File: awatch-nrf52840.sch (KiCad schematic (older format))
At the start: 22 parts, among them U1 nRF52840, X1 ABM11W-32.0000MHZ-8-B1U-T3

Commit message: add sensors
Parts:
- added R?: n/c, symbol Device:R_Small_US
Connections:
- net +2V8: now also R?.1
- net SENS_IMU_INT: now reaches U1.R24 (P1.06)
- net SENS_IMU_INT: now also R?.2
- no-connect marks 19 -> 18
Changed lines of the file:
@@
 NoConn ~ 5150 5000
 NoConn ~ 5150 5200
-NoConn ~ 5150 5800
 NoConn ~ 5150 5900
 NoConn ~ 5150 6000
@@
 Wire Wire Line
 	5800 4950 5800 5000
+Text HLabel 6700 5800 2    50   Input ~ 0
+SENS_IMU_INT
+Wire Wire Line
+	5150 5800 6200 5800
+$Comp
+L Device:R_Small_US R?
+U 1 1 5C442EC0
+P 6200 5100
+F 0 "R?" H 6268 5146 50  0000 L CNN
+F 1 "n/c" H 6268 5055 50  0000 L CNN
+F 2 "" H 6200 5100 50  0001 C CNN
+F 3 "~" H 6200 5100 50  0001 C CNN
+	1    6200 5100
+	1    0    0    -1
+$EndComp
+$Comp
+L power:+2V8 #PWR?
+U 1 1 5C44AE8F
+P 6200 4950
+F 0 "#PWR?" H 6200 4800 50  0001 C CNN
+F 1 "+2V8" H 6142 4987 50  0000 R CNN
+F 2 "" H 6200 4950 50  0001 C CNN
+F 3 "" H 6200 4950 50  0001 C CNN
+	1    6200 4950
+	1    0    0    -1
+$EndComp
+Wire Wire Line
+	6200 4950 6200 5000
+Wire Wire Line
+	6200 5200 6200 5800
 Wire Bus Line
 	5950 4000 5950 4400
+Connection ~ 6200 5800
+Wire Wire Line
+	6200 5800 6700 5800
 $EndSCHEMATC

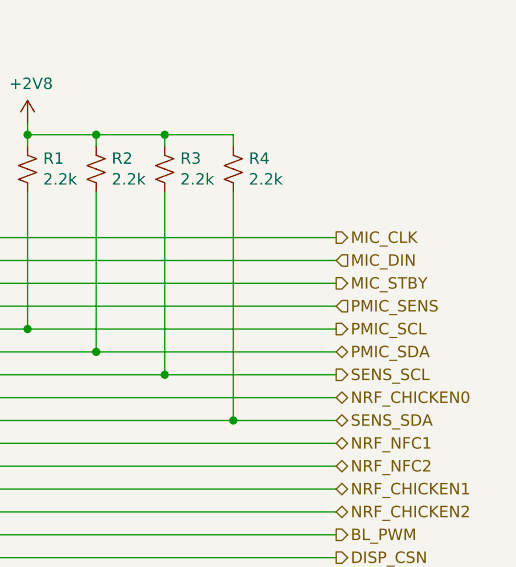
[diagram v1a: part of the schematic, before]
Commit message: add mic
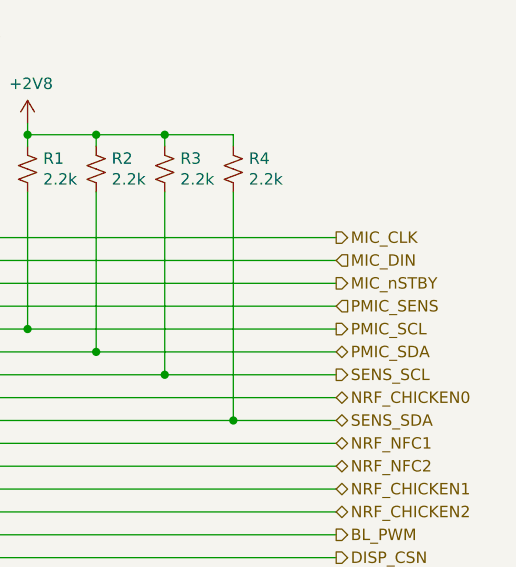
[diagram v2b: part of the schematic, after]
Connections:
- net MIC_STBY renamed MIC_nSTBY
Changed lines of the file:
@@
 $Descr A4 11693 8268
 encoding utf-8
-Sheet 2 5
+Sheet 2 6
 Title "AWatch2"
 Date ""
@@
 MIC_DIN
 Text HLabel 6700 2200 2    50   Output ~ 0
-MIC_STBY
+MIC_nSTBY
 Text HLabel 6700 2400 2    50   Output ~ 0
 PMIC_SCL

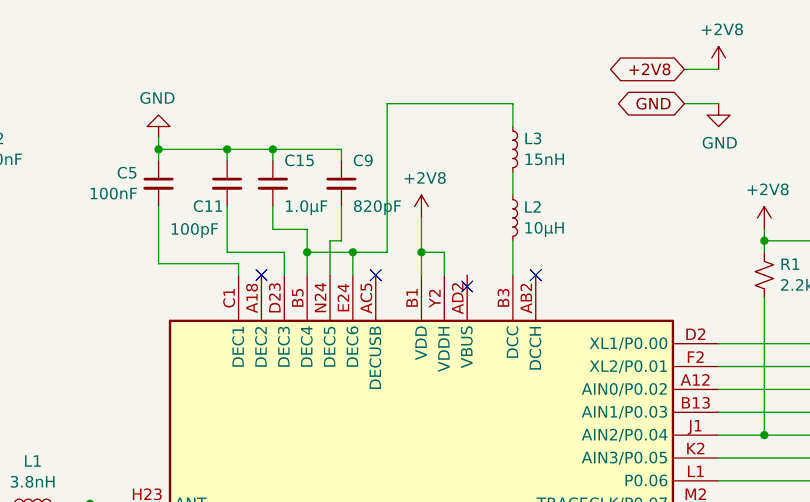
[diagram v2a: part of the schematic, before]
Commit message: Add display.  Add +3.3V LDO for backlight.
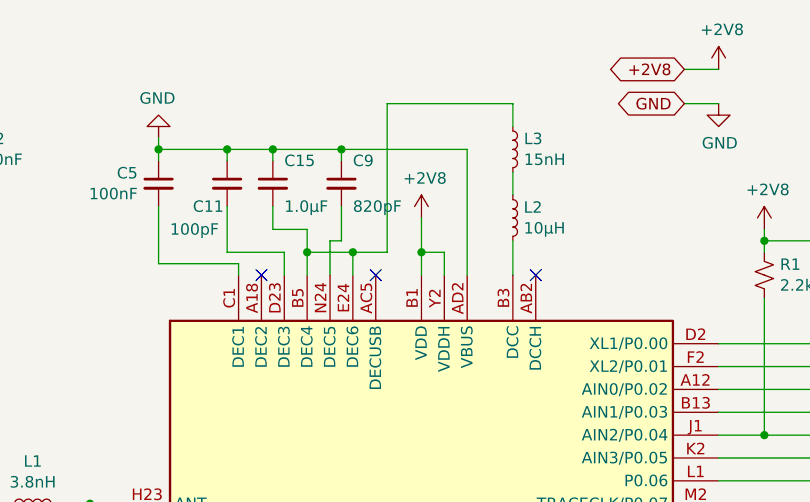
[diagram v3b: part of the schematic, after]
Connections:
- net GND: now also U1.AD2 (VBUS)
- no-connect marks 18 -> 17
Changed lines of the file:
@@
 $Descr A4 11693 8268
 encoding utf-8
-Sheet 2 6
+Sheet 2 7
 Title "AWatch2"
 Date ""
@@
 NoConn ~ 5150 7000
 NoConn ~ 4350 1700
-NoConn ~ 4050 1750
 NoConn ~ 3150 1700
 NoConn ~ 3650 1700
@@
 Wire Wire Line
 	6200 5200 6200 5800
+Connection ~ 6200 5800
+Wire Wire Line
+	6200 5800 6700 5800
+Wire Wire Line
+	4050 1700 4050 1150
+Wire Wire Line
+	4050 1150 3500 1150
 Wire Bus Line
 	5950 4000 5950 4400
-Connection ~ 6200 5800
-Wire Wire Line
-	6200 5800 6700 5800
+Connection ~ 3500 1150
 $EndSCHEMATC

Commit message: add FTDI
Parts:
- C1, C2: value 12pF -> 10pF
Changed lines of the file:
@@
 $Descr A4 11693 8268
 encoding utf-8
-Sheet 2 7
+Sheet 2 8
 Title "AWatch2"
 Date ""
@@
 P 2200 5000
 F 0 "C1" H 2086 5046 50  0000 R CNN
-F 1 "12pF" H 2086 4955 50  0000 R CNN
+F 1 "10pF" H 2086 4955 50  0000 R CNN
 F 2 "" H 2238 4850 50  0001 C CNN
 F 3 "~" H 2200 5000 50  0001 C CNN
@@
 P 2500 5000
 F 0 "C2" H 2615 5046 50  0000 L CNN
-F 1 "12pF" H 2615 4955 50  0000 L CNN
+F 1 "10pF" H 2615 4955 50  0000 L CNN
 F 2 "" H 2538 4850 50  0001 C CNN
 F 3 "~" H 2500 5000 50  0001 C CNN

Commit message: annotate all
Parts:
- gave numbers to parts that had none: 2
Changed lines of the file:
@@
 	5150 5700 5800 5700
 $Comp
-L Device:R_Small_US R?
+L Device:R_Small_US R201
 U 1 1 5C396EAC
 P 5800 5100
-F 0 "R?" H 5868 5146 50  0000 L CNN
+F 0 "R201" H 5868 5146 50  0000 L CNN
 F 1 "10k" H 5868 5055 50  0000 L CNN
 F 2 "" H 5800 5100 50  0001 C CNN
@@
 PMIC_INTn
 $Comp
-L power:+2V8 #PWR?
+L power:+2V8 #PWR0120
 U 1 1 5C39B10C
 P 5800 4950
-F 0 "#PWR?" H 5800 4800 50  0001 C CNN
+F 0 "#PWR0120" H 5800 4800 50  0001 C CNN
 F 1 "+2V8" H 5742 4987 50  0000 R CNN
 F 2 "" H 5800 4950 50  0001 C CNN
@@
 	5150 5800 6200 5800
 $Comp
-L Device:R_Small_US R?
+L Device:R_Small_US R202
 U 1 1 5C442EC0
 P 6200 5100
-F 0 "R?" H 6268 5146 50  0000 L CNN
+F 0 "R202" H 6268 5146 50  0000 L CNN
 F 1 "n/c" H 6268 5055 50  0000 L CNN
 F 2 "" H 6200 5100 50  0001 C CNN
@@
 $EndComp
 $Comp
-L power:+2V8 #PWR?
+L power:+2V8 #PWR0121
 U 1 1 5C44AE8F
 P 6200 4950
-F 0 "#PWR?" H 6200 4800 50  0001 C CNN
+F 0 "#PWR0121" H 6200 4800 50  0001 C CNN
 F 1 "+2V8" H 6142 4987 50  0000 R CNN
 F 2 "" H 6200 4950 50  0001 C CNN

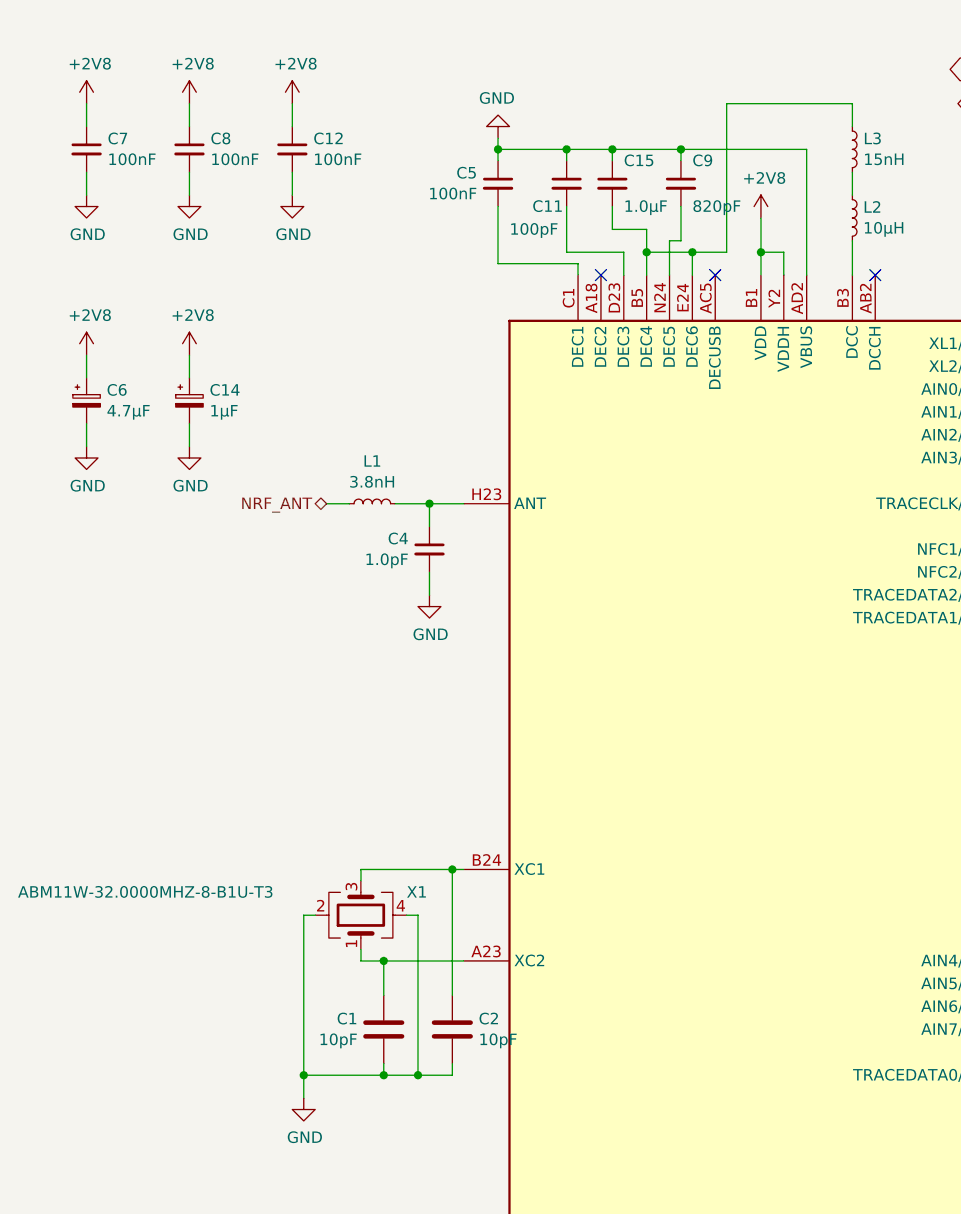
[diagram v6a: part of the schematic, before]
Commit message: Add footprints.
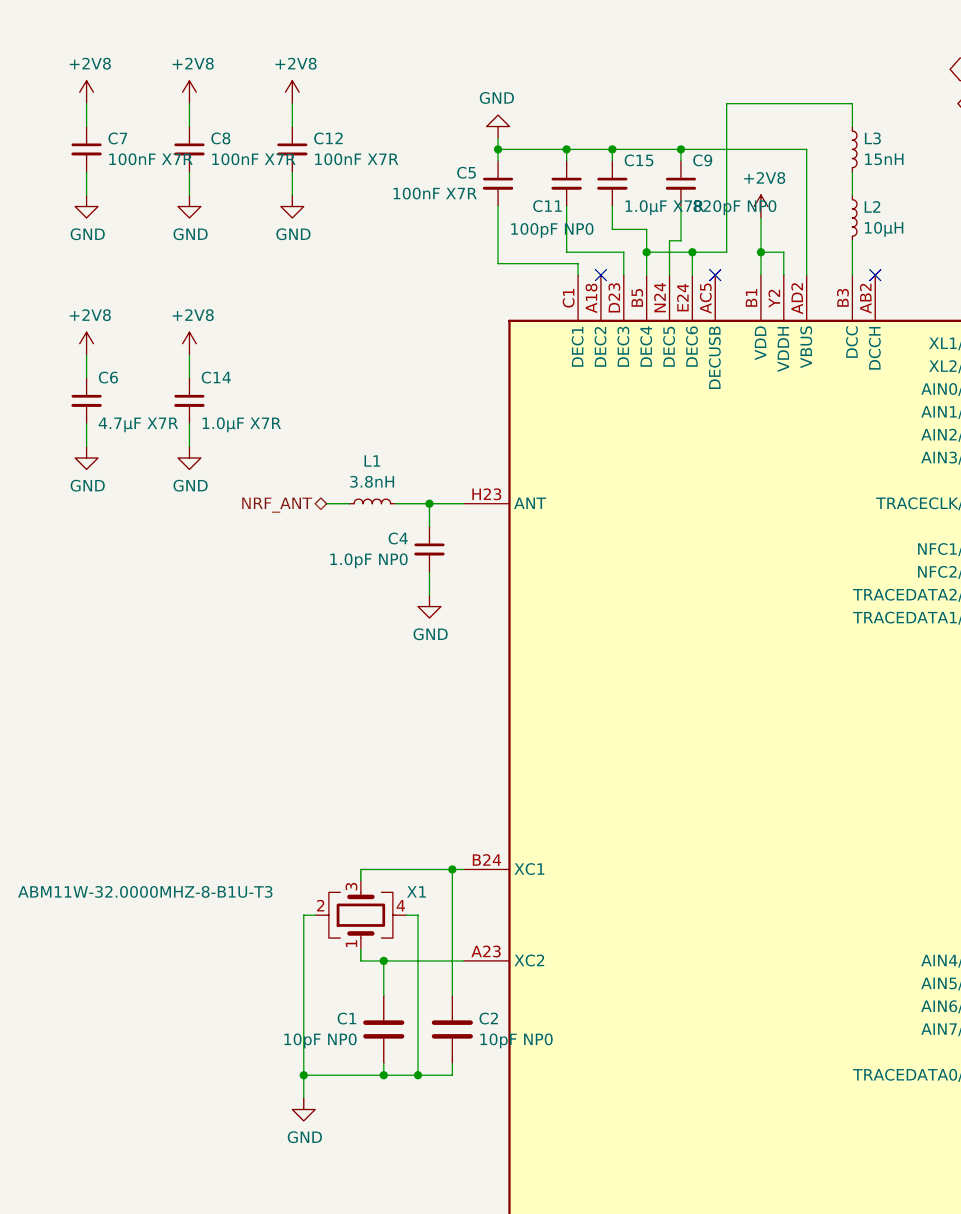
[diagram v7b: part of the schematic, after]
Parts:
- removed C14: 1µF, symbol Device:CP_Small
- removed C6: 4.7µF, symbol Device:CP_Small
- added C14: 1.0µF X7R, Capacitor_SMD:C_0603_1608Metric, symbol Device:C_Small
- added C6: 4.7µF X7R, Capacitor_SMD:C_0603_1608Metric, symbol Device:C_Small
- C1, C2: value 10pF -> 10pF NP0; footprint (none) -> Capacitor_SMD:C_0603_1608Metric
- C11: value 100pF -> 100pF NP0; footprint (none) -> Capacitor_SMD:C_0603_1608Metric
- C12, C5, C7, C8: value 100nF -> 100nF X7R; footprint (none) -> Capacitor_SMD:C_0603_1608Metric
- C15: value 1.0µF -> 1.0µF X7R; footprint (none) -> Capacitor_SMD:C_0603_1608Metric
- C4: value 1.0pF -> 1.0pF NP0; footprint (none) -> Capacitor_SMD:C_0603_1608Metric
- C9: value 820pF -> 820pF NP0; footprint (none) -> Capacitor_SMD:C_0603_1608Metric
- L1, L2, L3: footprint (none) -> Inductor_SMD:L_0603_1608Metric
- R1, R2, R201, R202, R3, R4: footprint (none) -> Resistor_SMD:R_0603_1608Metric
- X1: footprint (none) -> Crystal:Crystal_SMD_2016-4Pin_2.0x1.6mm
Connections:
- net +2V8: now also C14.1, C6.1
- net GND: now also C14.2, C6.2
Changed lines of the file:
@@
 EESchema Schematic File Version 4
+LIBS:awatch2-cache
 EELAYER 26 0
 EELAYER END
@@
 F 0 "X1" V 2200 4300 50  0000 R CNN
 F 1 "ABM11W-32.0000MHZ-8-B1U-T3" V 2200 6000 50  0000 R CNN
-F 2 "" H 2100 4500 50  0001 C CNN
+F 2 "Crystal:Crystal_SMD_2016-4Pin_2.0x1.6mm" H 2100 4500 50  0001 C CNN
 F 3 "~" H 2100 4500 50  0001 C CNN
 	1    2100 4500
@@
 P 2200 5000
 F 0 "C1" H 2086 5046 50  0000 R CNN
-F 1 "10pF" H 2086 4955 50  0000 R CNN
-F 2 "" H 2238 4850 50  0001 C CNN
+F 1 "10pF NP0" H 2086 4955 50  0000 R CNN
+F 2 "Capacitor_SMD:C_0603_1608Metric" H 2238 4850 50  0001 C CNN
 F 3 "~" H 2200 5000 50  0001 C CNN
 	1    2200 5000
@@
 P 2500 5000
 F 0 "C2" H 2615 5046 50  0000 L CNN
-F 1 "10pF" H 2615 4955 50  0000 L CNN
-F 2 "" H 2538 4850 50  0001 C CNN
+F 1 "10pF NP0" H 2615 4955 50  0000 L CNN
+F 2 "Capacitor_SMD:C_0603_1608Metric" H 2538 4850 50  0001 C CNN
 F 3 "~" H 2500 5000 50  0001 C CNN
 	1    2500 5000
@@
 P 2700 1300
 F 0 "C5" H 2609 1346 50  0000 R CNN
-F 1 "100nF" H 2609 1255 50  0000 R CNN
-F 2 "" H 2700 1300 50  0001 C CNN
+F 1 "100nF X7R" H 2609 1255 50  0000 R CNN
+F 2 "Capacitor_SMD:C_0603_1608Metric" H 2700 1300 50  0001 C CNN
 F 3 "~" H 2700 1300 50  0001 C CNN
 	1    2700 1300
@@
 P 3000 1300
 F 0 "C11" H 2850 1200 50  0000 L CNN
-F 1 "100pF" H 2750 1100 50  0000 L CNN
-F 2 "" H 3000 1300 50  0001 C CNN
+F 1 "100pF NP0" H 2750 1100 50  0000 L CNN
+F 2 "Capacitor_SMD:C_0603_1608Metric" H 3000 1300 50  0001 C CNN
 F 3 "~" H 3000 1300 50  0001 C CNN
 	1    3000 1300
@@
 P 3200 1300
 F 0 "C15" H 3250 1400 50  0000 L CNN
-F 1 "1.0µF" H 3250 1200 50  0000 L CNN
-F 2 "" H 3200 1300 50  0001 C CNN
+F 1 "1.0µF X7R" H 3250 1200 50  0000 L CNN
+F 2 "Capacitor_SMD:C_0603_1608Metric" H 3200 1300 50  0001 C CNN
 F 3 "~" H 3200 1300 50  0001 C CNN
 	1    3200 1300
@@
 P 3500 1300
 F 0 "C9" H 3550 1400 50  0000 L CNN
-F 1 "820pF" H 3550 1200 50  0000 L CNN
-F 2 "" H 3500 1300 50  0001 C CNN
+F 1 "820pF NP0" H 3550 1200 50  0000 L CNN
+F 2 "Capacitor_SMD:C_0603_1608Metric" H 3500 1300 50  0001 C CNN
 F 3 "~" H 3500 1300 50  0001 C CNN
 	1    3500 1300
@@
 F 0 "L2" H 4297 1496 50  0000 L CNN
 F 1 "10µH" H 4297 1405 50  0000 L CNN
-F 2 "" H 4250 1450 50  0001 C CNN
+F 2 "Inductor_SMD:L_0603_1608Metric" H 4250 1450 50  0001 C CNN
 F 3 "~" H 4250 1450 50  0001 C CNN
 	1    4250 1450
@@
 F 0 "L3" H 4298 1196 50  0000 L CNN
 F 1 "15nH" H 4298 1105 50  0000 L CNN
-F 2 "" H 4250 1150 50  0001 C CNN
+F 2 "Inductor_SMD:L_0603_1608Metric" H 4250 1150 50  0001 C CNN
 F 3 "~" H 4250 1150 50  0001 C CNN
 	1    4250 1150
@@
 P 900 1150
 F 0 "C7" H 992 1196 50  0000 L CNN
-F 1 "100nF" H 992 1105 50  0000 L CNN
-F 2 "" H 900 1150 50  0001 C CNN
+F 1 "100nF X7R" H 992 1105 50  0000 L CNN
+F 2 "Capacitor_SMD:C_0603_1608Metric" H 900 1150 50  0001 C CNN
 F 3 "~" H 900 1150 50  0001 C CNN
 	1    900  1150
@@
 P 1350 1150
 F 0 "C8" H 1442 1196 50  0000 L CNN
-F 1 "100nF" H 1442 1105 50  0000 L CNN
-F 2 "" H 1350 1150 50  0001 C CNN
+F 1 "100nF X7R" H 1442 1105 50  0000 L CNN
+F 2 "Capacitor_SMD:C_0603_1608Metric" H 1350 1150 50  0001 C CNN
 F 3 "~" H 1350 1150 50  0001 C CNN
 	1    1350 1150
@@
 P 1800 1150
 F 0 "C12" H 1892 1196 50  0000 L CNN
-F 1 "100nF" H 1892 1105 50  0000 L CNN
-F 2 "" H 1800 1150 50  0001 C CNN
+F 1 "100nF X7R" H 1892 1105 50  0000 L CNN
+F 2 "Capacitor_SMD:C_0603_1608Metric" H 1800 1150 50  0001 C CNN
 F 3 "~" H 1800 1150 50  0001 C CNN
 	1    1800 1150
@@
 	900  950  900  1050
 $Comp
-L Device:CP_Small C6
-U 1 1 5C26B3DB
-P 900 2250
-F 0 "C6" H 988 2296 50  0000 L CNN
-F 1 "4.7µF" H 988 2205 50  0000 L CNN
-F 2 "" H 900 2250 50  0001 C CNN
-F 3 "~" H 900 2250 50  0001 C CNN
-	1    900  2250
-	1    0    0    -1
-$EndComp
-$Comp
-L Device:CP_Small C14
-U 1 1 5C26B5E8
-P 1350 2250
-F 0 "C14" H 1438 2296 50  0000 L CNN
-F 1 "1µF" H 1438 2205 50  0000 L CNN
-F 2 "" H 1350 2250 50  0001 C CNN
-F 3 "~" H 1350 2250 50  0001 C CNN
-	1    1350 2250
-	1    0    0    -1
-$EndComp
-$Comp
 L Device:C_Small C4
 U 1 1 5C26D362
 P 2400 2900
 F 0 "C4" H 2309 2946 50  0000 R CNN
-F 1 "1.0pF" H 2309 2855 50  0000 R CNN
-F 2 "" H 2400 2900 50  0001 C CNN
+F 1 "1.0pF NP0" H 2309 2855 50  0000 R CNN
+F 2 "Capacitor_SMD:C_0603_1608Metric" H 2400 2900 50  0001 C CNN
 F 3 "~" H 2400 2900 50  0001 C CNN
 	1    2400 2900
@@
 F 0 "L1" V 2335 2700 50  0000 C CNN
 F 1 "3.8nH" V 2244 2700 50  0000 C CNN
-F 2 "" H 2150 2700 50  0001 C CNN
+F 2 "Inductor_SMD:L_0603_1608Metric" H 2150 2700 50  0001 C CNN
 F 3 "~" H 2150 2700 50  0001 C CNN
 	1    2150 2700
@@
 F 0 "R1" H 5418 1746 50  0000 L CNN
 F 1 "2.2k" H 5418 1655 50  0000 L CNN
-F 2 "" H 5350 1700 50  0001 C CNN
+F 2 "Resistor_SMD:R_0603_1608Metric" H 5350 1700 50  0001 C CNN
 F 3 "~" H 5350 1700 50  0001 C CNN
 	1    5350 1700
@@
 F 0 "R2" H 5718 1746 50  0000 L CNN
 F 1 "2.2k" H 5718 1655 50  0000 L CNN
-F 2 "" H 5650 1700 50  0001 C CNN
+F 2 "Resistor_SMD:R_0603_1608Metric" H 5650 1700 50  0001 C CNN
 F 3 "~" H 5650 1700 50  0001 C CNN
 	1    5650 1700
@@
 F 0 "R3" H 6018 1746 50  0000 L CNN
 F 1 "2.2k" H 6018 1655 50  0000 L CNN
-F 2 "" H 5950 1700 50  0001 C CNN
+F 2 "Resistor_SMD:R_0603_1608Metric" H 5950 1700 50  0001 C CNN
 F 3 "~" H 5950 1700 50  0001 C CNN
 	1    5950 1700
@@
 F 0 "R4" H 6318 1746 50  0000 L CNN
 F 1 "2.2k" H 6318 1655 50  0000 L CNN
-F 2 "" H 6250 1700 50  0001 C CNN
+F 2 "Resistor_SMD:R_0603_1608Metric" H 6250 1700 50  0001 C CNN
 F 3 "~" H 6250 1700 50  0001 C CNN
 	1    6250 1700
@@
 F 0 "R201" H 5868 5146 50  0000 L CNN
 F 1 "10k" H 5868 5055 50  0000 L CNN
-F 2 "" H 5800 5100 50  0001 C CNN
+F 2 "Resistor_SMD:R_0603_1608Metric" H 5800 5100 50  0001 C CNN
 F 3 "~" H 5800 5100 50  0001 C CNN
 	1    5800 5100
@@
 F 0 "R202" H 6268 5146 50  0000 L CNN
 F 1 "n/c" H 6268 5055 50  0000 L CNN
-F 2 "" H 6200 5100 50  0001 C CNN
+F 2 "Resistor_SMD:R_0603_1608Metric" H 6200 5100 50  0001 C CNN
 F 3 "~" H 6200 5100 50  0001 C CNN
 	1    6200 5100
@@
 Wire Wire Line
 	4050 1150 3500 1150
+Connection ~ 3500 1150
+$Comp
+L Device:C_Small C14
+U 1 1 5C857E99
+P 1350 2250
+F 0 "C14" H 1400 2350 50  0000 L CNN
+F 1 "1.0µF X7R" H 1400 2150 50  0000 L CNN
+F 2 "Capacitor_SMD:C_0603_1608Metric" H 1350 2250 50  0001 C CNN
+F 3 "~" H 1350 2250 50  0001 C CNN
+	1    1350 2250
+	1    0    0    -1
+$EndComp
 Wire Bus Line
 	5950 4000 5950 4400
-Connection ~ 3500 1150
+$Comp
+L Device:C_Small C6
+U 1 1 5C2C501B
+P 900 2250
+F 0 "C6" H 950 2350 50  0000 L CNN
+F 1 "4.7µF X7R" H 950 2150 50  0000 L CNN
+F 2 "Capacitor_SMD:C_0603_1608Metric" H 900 2250 50  0001 C CNN
+F 3 "~" H 900 2250 50  0001 C CNN
+	1    900  2250
+	1    0    0    -1
+$EndComp
 $EndSCHEMATC

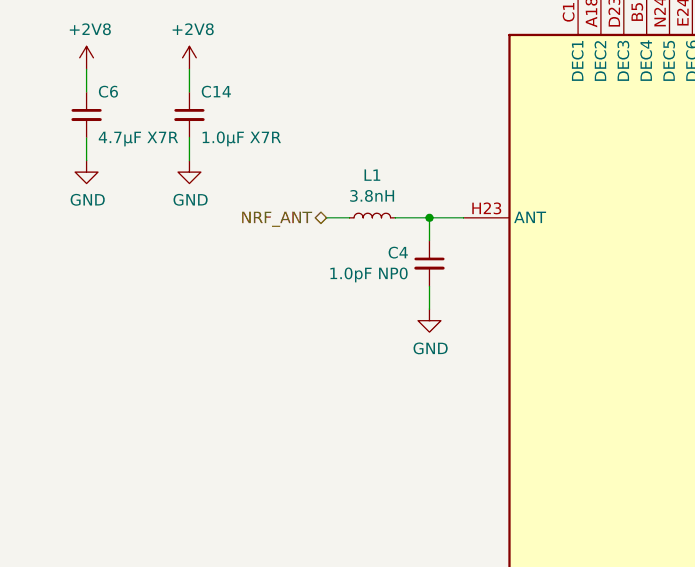
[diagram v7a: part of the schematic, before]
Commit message: relative placement and routing for nRF52840
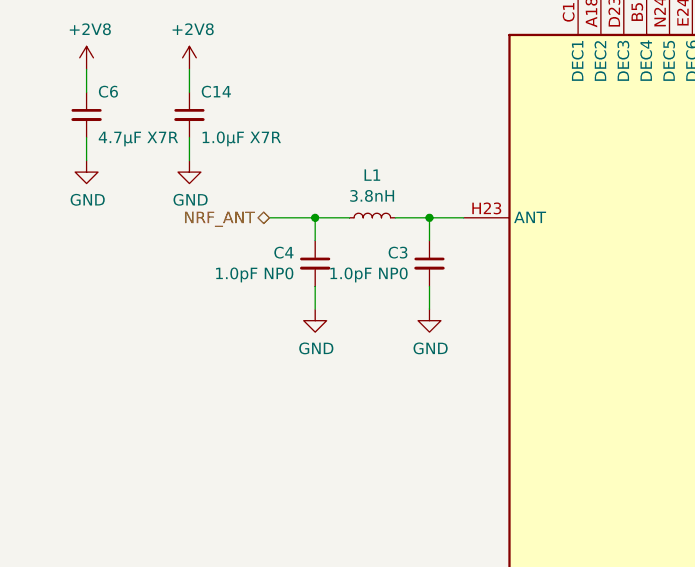
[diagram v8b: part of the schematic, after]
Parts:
- added C4: 1.0pF NP0, Capacitor_SMD:C_0603_1608Metric, symbol Device:C_Small
- renumbered C4 to C3
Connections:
- net GND: now also C4.2
- net NRF_ANT: now also C4.1
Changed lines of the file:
@@
 	900  950  900  1050
 $Comp
-L Device:C_Small C4
+L Device:C_Small C3
 U 1 1 5C26D362
 P 2400 2900
-F 0 "C4" H 2309 2946 50  0000 R CNN
+F 0 "C3" H 2309 2946 50  0000 R CNN
 F 1 "1.0pF NP0" H 2309 2855 50  0000 R CNN
 F 2 "Capacitor_SMD:C_0603_1608Metric" H 2400 2900 50  0001 C CNN
@@
 Wire Wire Line
 	2400 3000 2400 3100
-Text HLabel 1950 2700 0    50   BiDi ~ 0
+Text HLabel 1700 2700 0    50   BiDi ~ 0
 NRF_ANT
-Wire Wire Line
-	1950 2700 2050 2700
 Text Label 6050 4400 0    50   ~ 0
 FLASH_D[0..3]
@@
 	1    0    0    -1
 $EndComp
-Wire Bus Line
-	5950 4000 5950 4400
 $Comp
 L Device:C_Small C6
@@
 	1    0    0    -1
 $EndComp
+$Comp
+L Device:C_Small C4
+U 1 1 5C319D98
+P 1900 2900
+F 0 "C4" H 1809 2946 50  0000 R CNN
+F 1 "1.0pF NP0" H 1809 2855 50  0000 R CNN
+F 2 "Capacitor_SMD:C_0603_1608Metric" H 1900 2900 50  0001 C CNN
+F 3 "~" H 1900 2900 50  0001 C CNN
+	1    1900 2900
+	1    0    0    -1
+$EndComp
+Wire Wire Line
+	1700 2700 1900 2700
+Wire Wire Line
+	1900 2700 1900 2800
+Connection ~ 1900 2700
+Wire Wire Line
+	1900 2700 2050 2700
+$Comp
+L power:GND #PWR?
+U 1 1 5C322A37
+P 1900 3100
+F 0 "#PWR?" H 1900 2850 50  0001 C CNN
+F 1 "GND" H 1905 2927 50  0000 C CNN
+F 2 "" H 1900 3100 50  0001 C CNN
+F 3 "" H 1900 3100 50  0001 C CNN
+	1    1900 3100
+	1    0    0    -1
+$EndComp
+Wire Wire Line
+	1900 3000 1900 3100
+Wire Bus Line
+	5950 4000 5950 4400
 $EndSCHEMATC
